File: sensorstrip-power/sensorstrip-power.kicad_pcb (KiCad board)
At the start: 2 copper layers, 42 x 15 mm, 20 parts, among them J1 USB_C_Receptacle_PowerOnly, J2 Conn_01x02_MountingPin, J3 Conn_01x02_MountingPin, J4 Conn_01x02_MountingPin, J5 Conn_01x02_MountingPin, SW1 SW_DPDT_x2

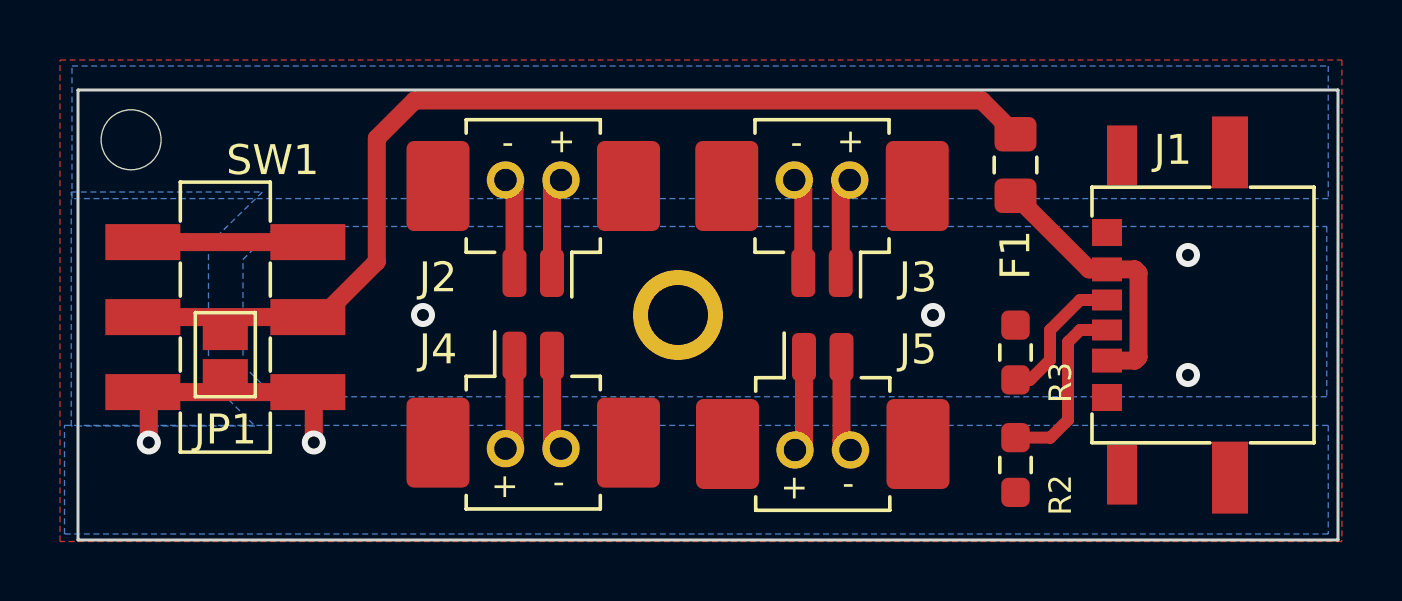
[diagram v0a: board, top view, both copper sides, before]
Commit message: Cleanup in preparation for push
Update project files to KiCad 7 format
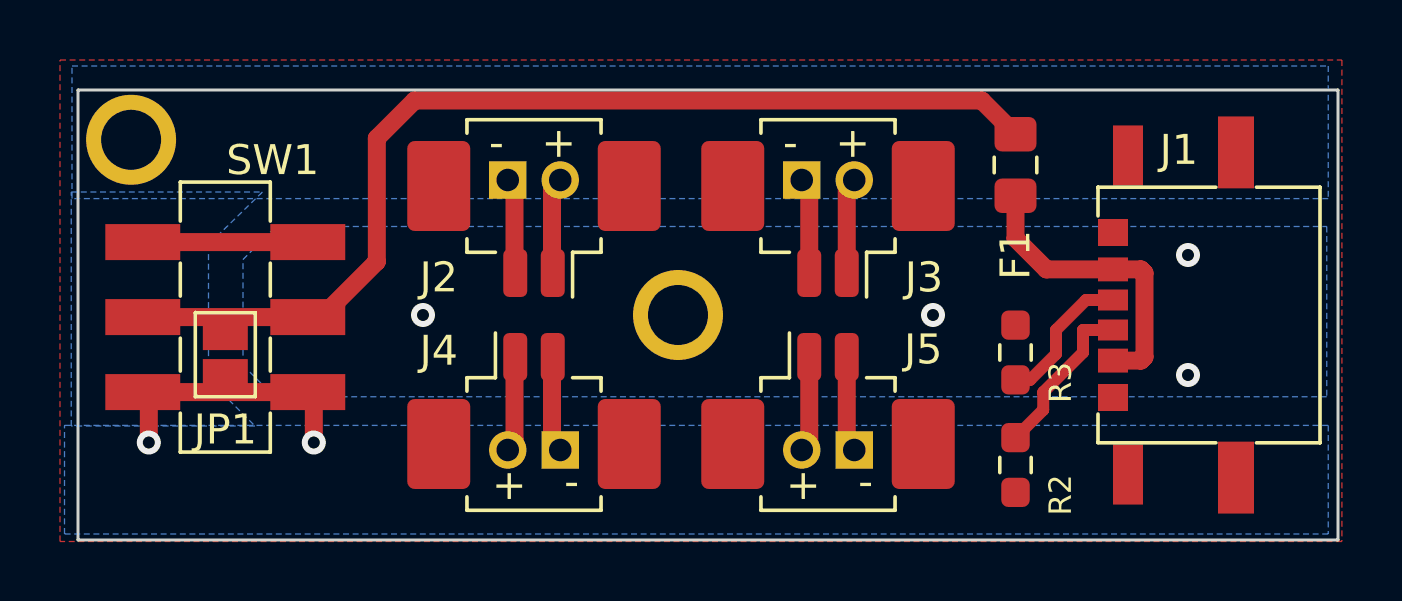
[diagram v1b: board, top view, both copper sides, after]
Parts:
- removed the ? at (116.1, 62.0)
- removed the ? at (125.8, 62.0)
- removed the ? at (123.9, 62.0)
- removed the ? at (123.9, 53.0)
- removed the ? at (114.6, 53.0)
- removed the ? at (114.2, 62.0)
- removed the ? at (125.7, 53.0)
- removed the ? at (116.1, 53.0)
- added REF**: Power-P1.75mm, sensorstrip:Power-P1.75mm, F.Cu at (125.0, 53.0)
- added REF**: Power-P1.75mm, sensorstrip:Power-P1.75mm, F.Cu at (115.2, 53.0)
- added REF**: Power-P1.75mm, sensorstrip:Power-P1.75mm, F.Cu at (115.2, 62.0)
- added REF**: Power-P1.75mm, sensorstrip:Power-P1.75mm, F.Cu at (125.0, 62.0)
- ? (x2): value (none) -> MountingHole-2mm-PTH; footprint (none) -> sensorstrip:MountingHole-2mm-PTH
- moved ? 0.25 mm to (120.0, 57.5)
- moved J1 0.20 mm to (134.5, 57.5)
- moved J3 0.20 mm to (125.0, 53.7)
- moved J5 0.17 mm to (125.0, 61.3)
- moved J4 0.05 mm to (115.2, 61.3)
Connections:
- SW1 pad 3: unconnected-(SW1-Pad3) -> Net-(SW1A-C)
- SW1 pad 6: unconnected-(SW1-Pad3) -> Net-(SW1A-C)
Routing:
- net unconnected-(SW1-Pad3): track 5.50 -> 0.00 mm
- net Net-(SW1A-C): track 0.00 -> 5.50 mm
- net GND: track 12.9 -> 11.7 mm
- net /VBUS: track 9.07 -> 10.1 mm
- net /CC1: track 6.06 -> 5.52 mm
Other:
- board text removed: "+"
- board text removed: "-"
